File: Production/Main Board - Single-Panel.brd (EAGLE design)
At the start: 186.9 x 255.3 mm, 534 parts, among them J1 MICROMOD-2222-C, J10 MICRO-SD-PUSH-PUSH-EXT-PIN, J11 MICROMOD-2222-C, J12 CORTEX_JTAG_DEBUG_MINIMUM_PTH, J15 MICROMOD_CARRIER, J16 MICRO-SD-PUSH-PUSH-EXT-PIN, J19 Vertical Qwiic Connector, J2 Vertical Qwiic Connector, J20 QWIIC_RIGHT_ANGLE, J21 MICROMOD-2222-C, J22 CORTEX_JTAG_DEBUG_MINIMUM_PTH, J24 MICROMOD_CARRIER, J25 MICRO-SD-PUSH-PUSH-EXT-PIN, J28 Vertical Qwiic Connector, J29 QWIIC_RIGHT_ANGLE, J30 MICROMOD-2222-C, J31 CORTEX_JTAG_DEBUG_MINIMUM_PTH, J33 MICROMOD_CARRIER, J34 MICRO-SD-PUSH-PUSH-EXT-PIN, J37 Vertical Qwiic Connector, J38 QWIIC_RIGHT_ANGLE, J39 MICROMOD-2222-C, J4 QWIIC_RIGHT_ANGLE, J40 CORTEX_JTAG_DEBUG_MINIMUM_PTH, J42 MICROMOD_CARRIER, J43 MICRO-SD-PUSH-PUSH-EXT-PIN, J46 Vertical Qwiic Connector, J47 QWIIC_RIGHT_ANGLE, J48 MICROMOD-2222-C, J49 CORTEX_JTAG_DEBUG_MINIMUM_PTH, J5 CORTEX_JTAG_DEBUG_MINIMUM_PTH, J51 MICROMOD_CARRIER, J52 MICRO-SD-PUSH-PUSH-EXT-PIN, J6 MICROMOD_CARRIER, J7 Vertical Qwiic Connector, J9 QWIIC_RIGHT_ANGLE, Q1 3.1A/30V/105mΩ, Q2 3.1A/30V/105mΩ, Q3 3.1A/30V/105mΩ, Q4 3.1A/30V/105mΩ, Q5 3.1A/30V/105mΩ, Q6 3.1A/30V/105mΩ, U1 AP7361C-33, U10 MCP73831, U11 AP7361C-33, U12 MCP73831, U2 MCP73831, U3 MCP73831, U4 AP7361C-33, U5 AP7361C-33, U6 MCP73831, U7 AP7361C-33, U8 MCP73831, U9 AP7361C-33

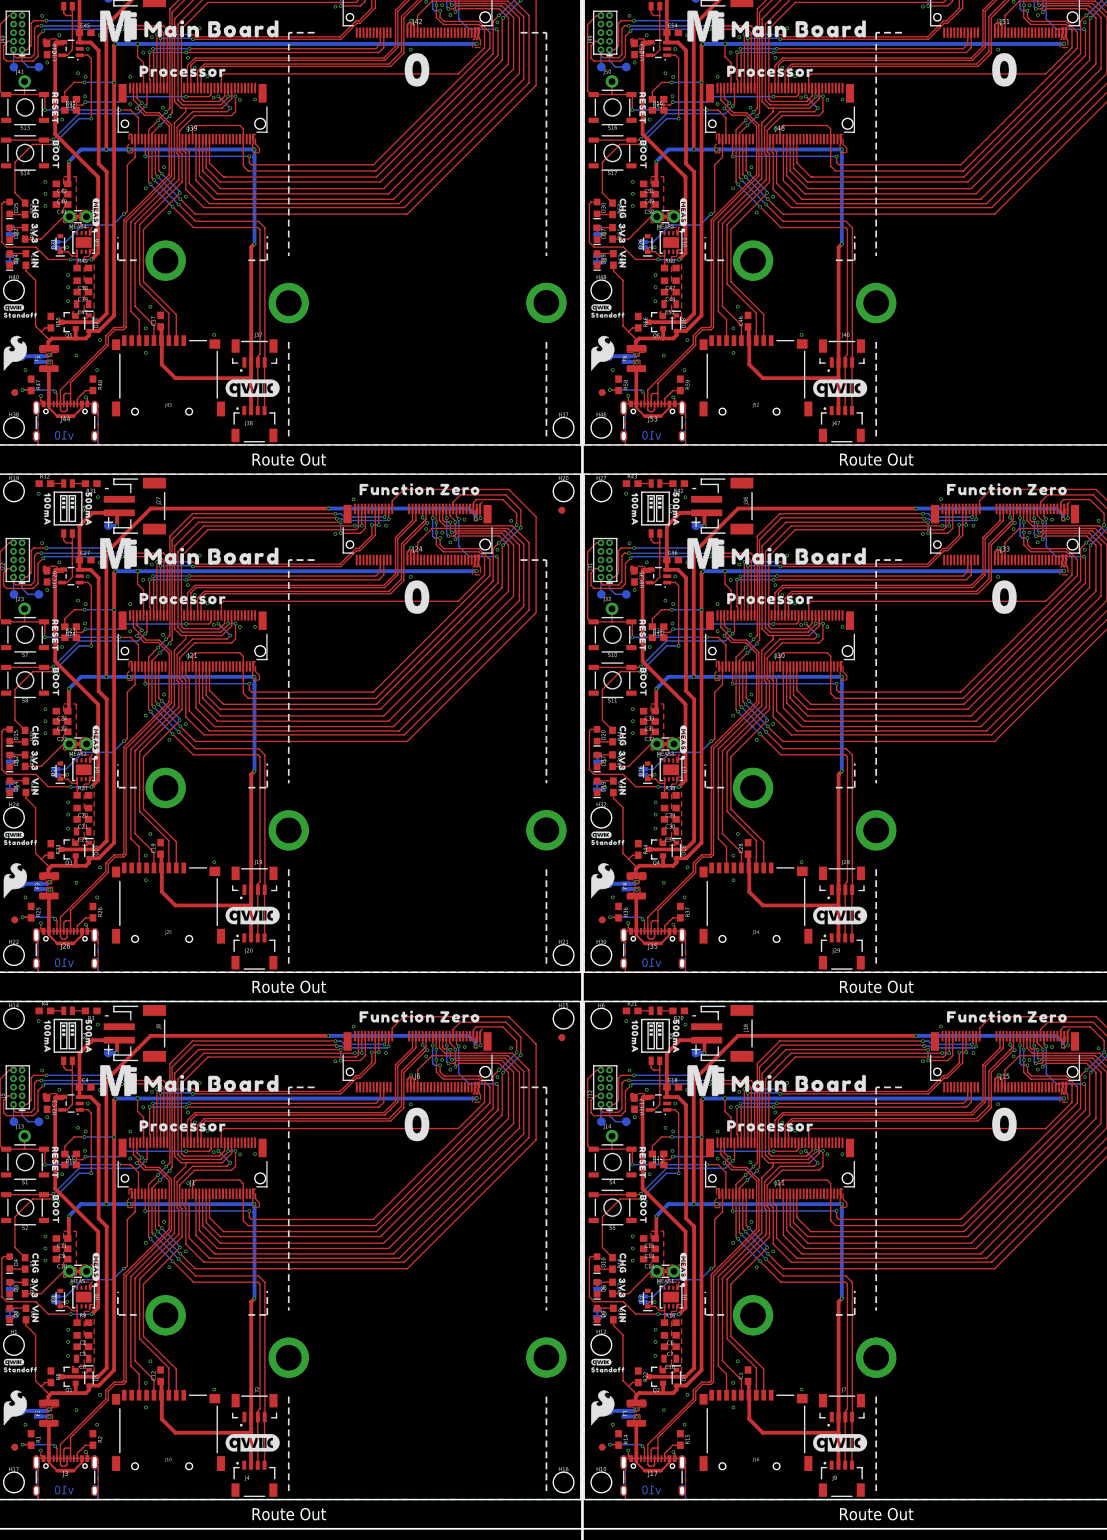
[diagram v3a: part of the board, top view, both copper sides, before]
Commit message: Adds new panel
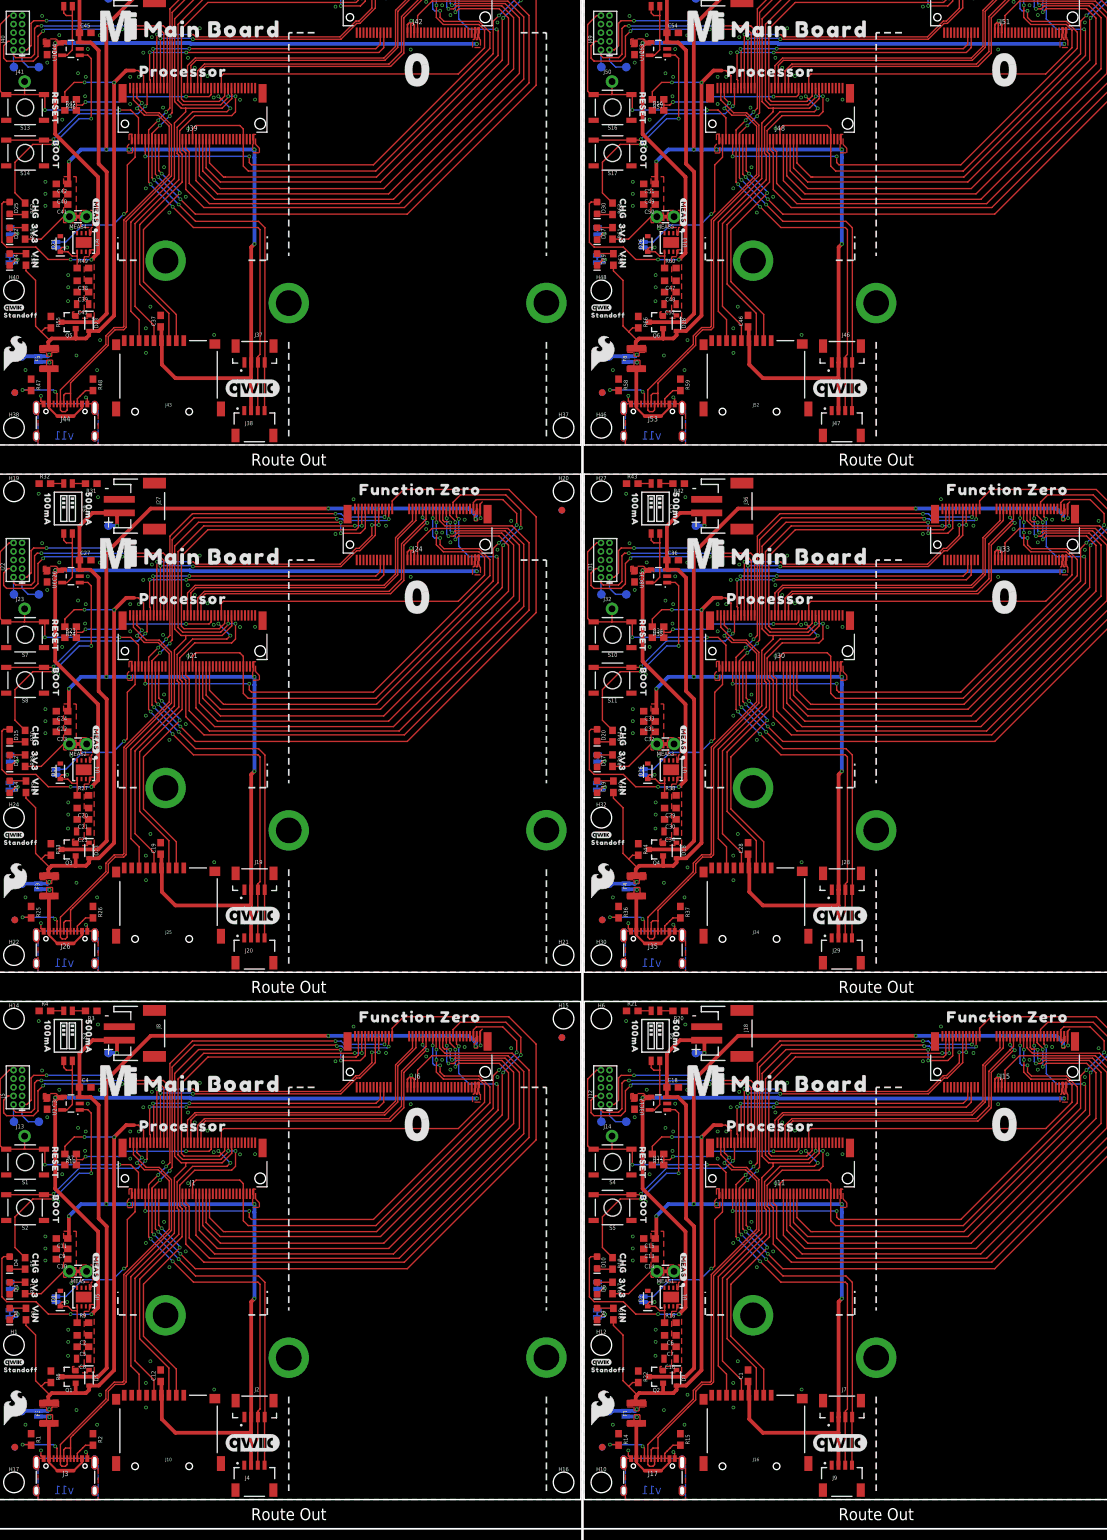
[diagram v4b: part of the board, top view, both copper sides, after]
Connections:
- net VCC: now also J6.72, J6.74
- net VCC1: now also J15.72, J15.74
- net VCC2: now also J24.72, J24.74
- net VCC3: now also J33.72, J33.74
- net VCC4: now also J42.72, J42.74
- net VCC5: now also J51.72, J51.74
- net VIN: no longer J6.72, J6.74
- net VIN1: no longer J15.72, J15.74
- net VIN2: no longer J24.72, J24.74
- net VIN3: no longer J33.72, J33.74
- net VIN4: no longer J42.72, J42.74
- net VIN5: no longer J51.72, J51.74
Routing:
- net VCC: track 57.4 -> 119.8 mm, vias 2 -> 4
- net VCC4: track 57.4 -> 119.8 mm, vias 2 -> 4
- net VCC5: track 57.4 -> 119.8 mm, vias 2 -> 4
- net VCC2: track 57.4 -> 119.8 mm, vias 2 -> 4
- net VCC1: track 57.4 -> 119.8 mm, vias 2 -> 4
- net VCC3: track 57.4 -> 119.8 mm, vias 2 -> 4
- net VIN5: track 142.2 -> 83.4 mm, vias 6 -> 3
- net VIN2: track 142.2 -> 83.4 mm, vias 6 -> 3
- net VIN4: track 142.2 -> 83.4 mm, vias 6 -> 3
- net VIN3: track 142.2 -> 83.4 mm, vias 6 -> 3
- net VIN1: track 142.2 -> 83.4 mm, vias 6 -> 3
- net VIN: track 142.2 -> 83.4 mm, vias 6 -> 3
- net GND5: vias 59 -> 60
- net GND4: vias 59 -> 60
- net GND3: vias 59 -> 60
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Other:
- board text added: "v11"
- board text removed: "v10"
